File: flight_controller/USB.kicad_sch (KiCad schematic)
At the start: 11 parts, among them J17 TYPE-C16PIN2MD(073) (USB TYPE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, U15 SN74LVC1G07DBVR_C19829659

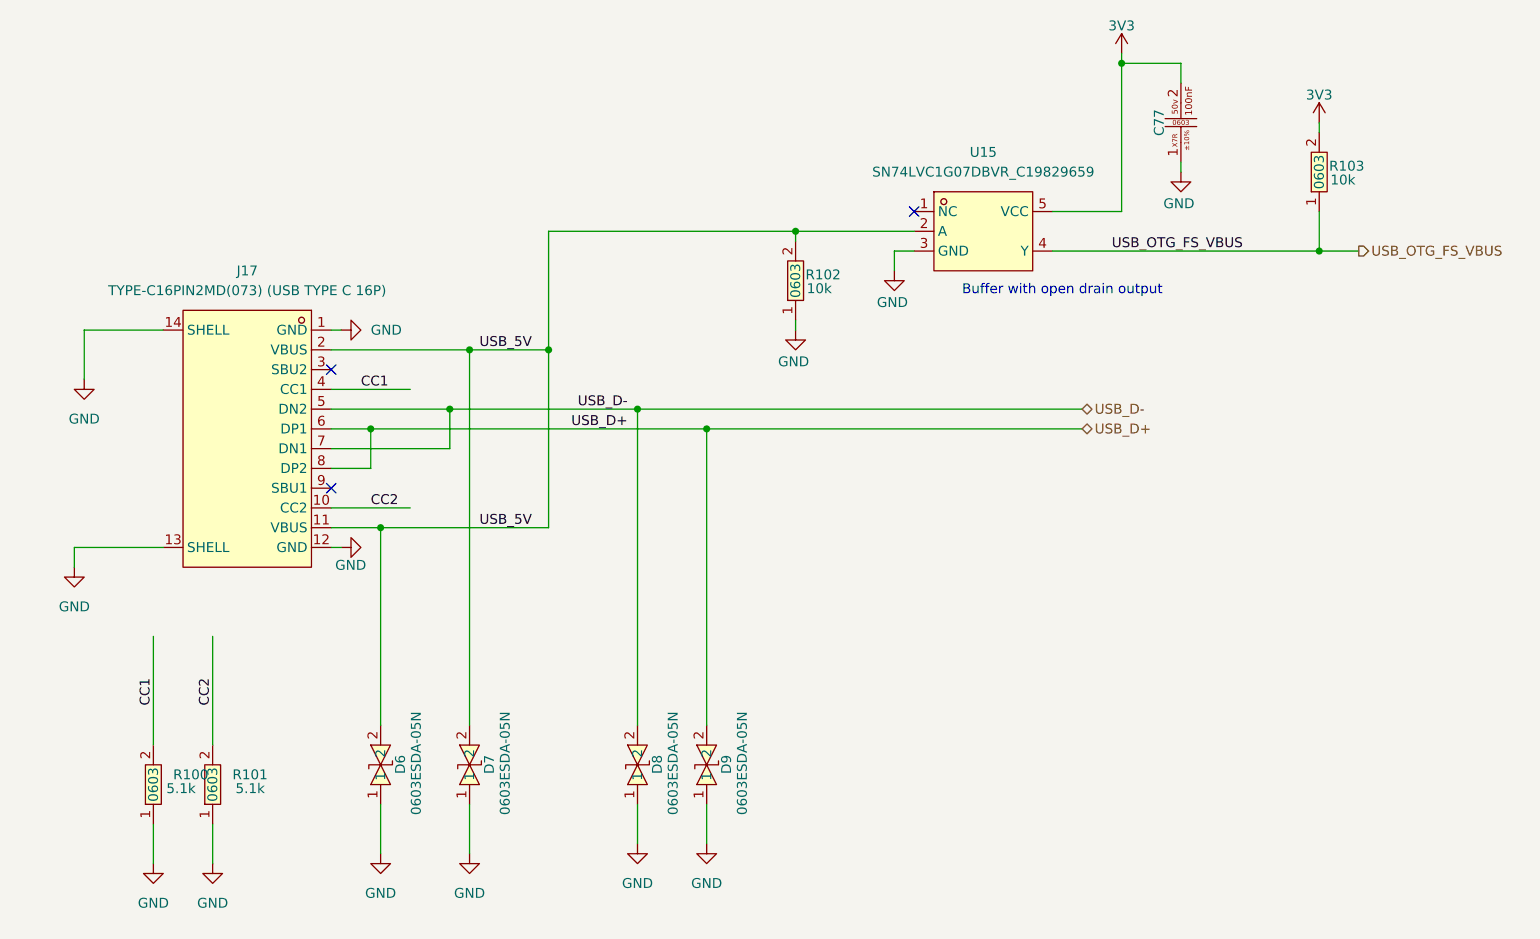
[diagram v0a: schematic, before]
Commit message: Updated power and usb connectors, annotations and netlist check
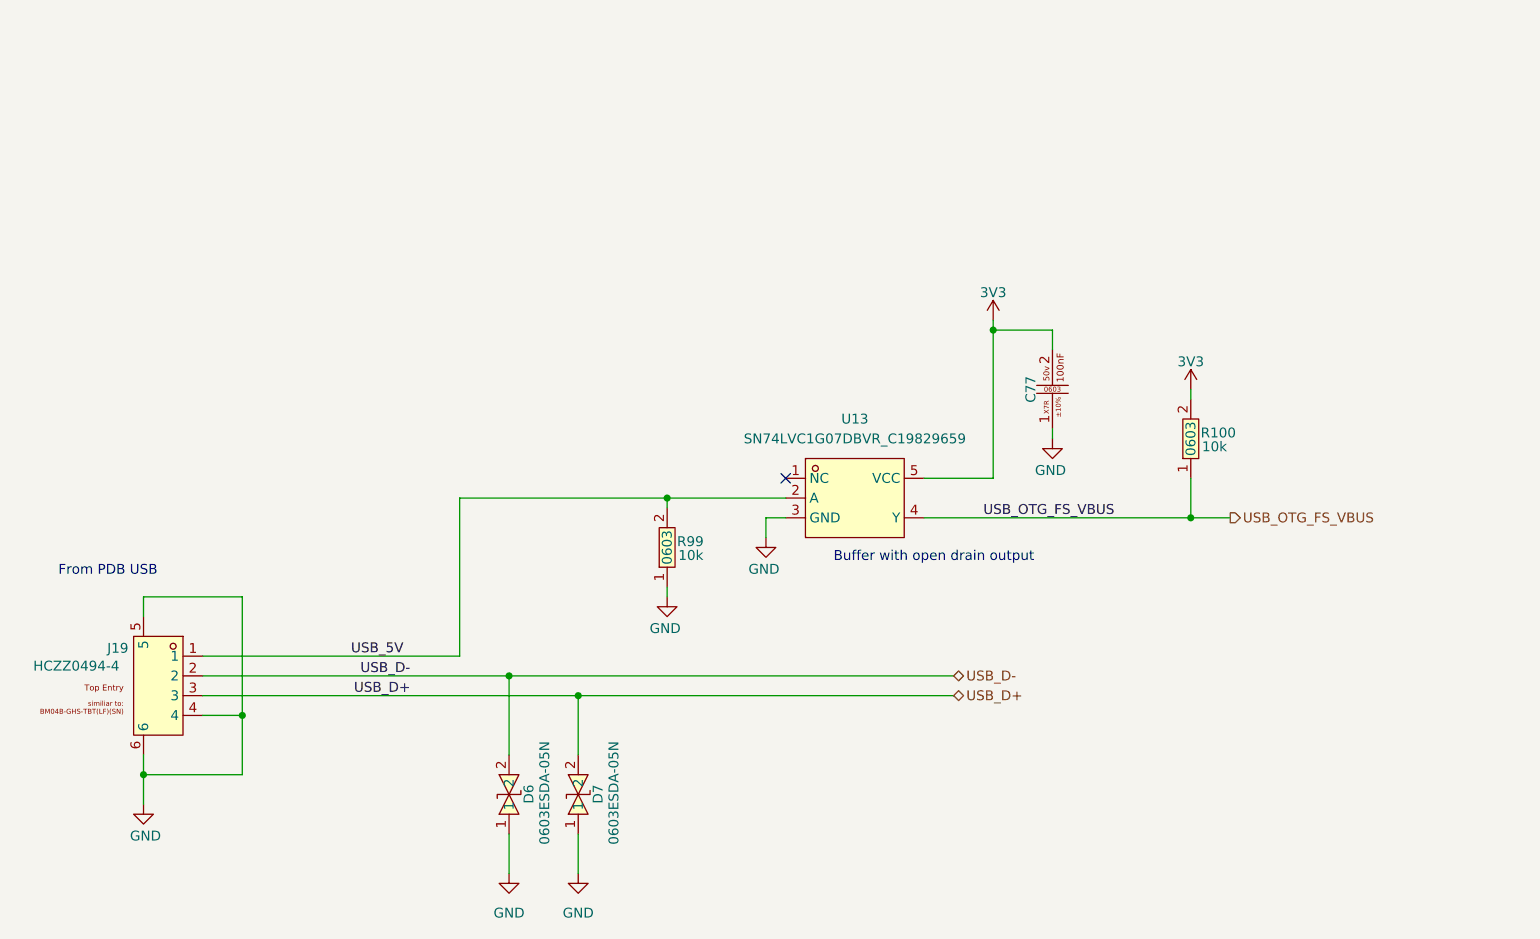
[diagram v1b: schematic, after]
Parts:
- removed D6, D7: 0603ESDA-05N, easyeda2kicad:D0603-BI, symbol easyeda2kicad:0603ESDA-05N
- removed J17: TYPE-C16PIN2MD(073) (USB TYPE C 16P), easyeda2kicad:USB-C-SMD_TYPE-C-6PIN-2MD-073, symbol lampelKicadLIB:TYPE-C16PIN2MD(073) (USB TYPE C 16P)
- removed R100, R101: 0603WAF5101T5E, easyeda2kicad:R0603, symbol easyeda2kicad:0603WAF5101T5E
- added J19: HCZZ0494-4, easyeda2kicad:CONN-SMD_4P-P1.25_BM04B-GHS-TBT-LF-SN, symbol lampelKicadLIB:HCZZ0494-4
- renumbered D8 to D6, D9 to D7, R103 to R100, R102 to R99, U15 to U13
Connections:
- net GND: now also J19.4, J19.5, J19.6
- net USB_5V: now also J19.1
- net USB_D+: now also J19.3
- net USB_D-: now also J19.2
- no-connect marks 3 -> 1
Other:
- note added: "From PDB USB"
- moved on the sheet: C77, D6, D7, R100, R99, U13

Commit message: Revert to state of commit 2458262 moved all to components to top
Reverts commits: d012532, 3d9c600, 58bc0ac
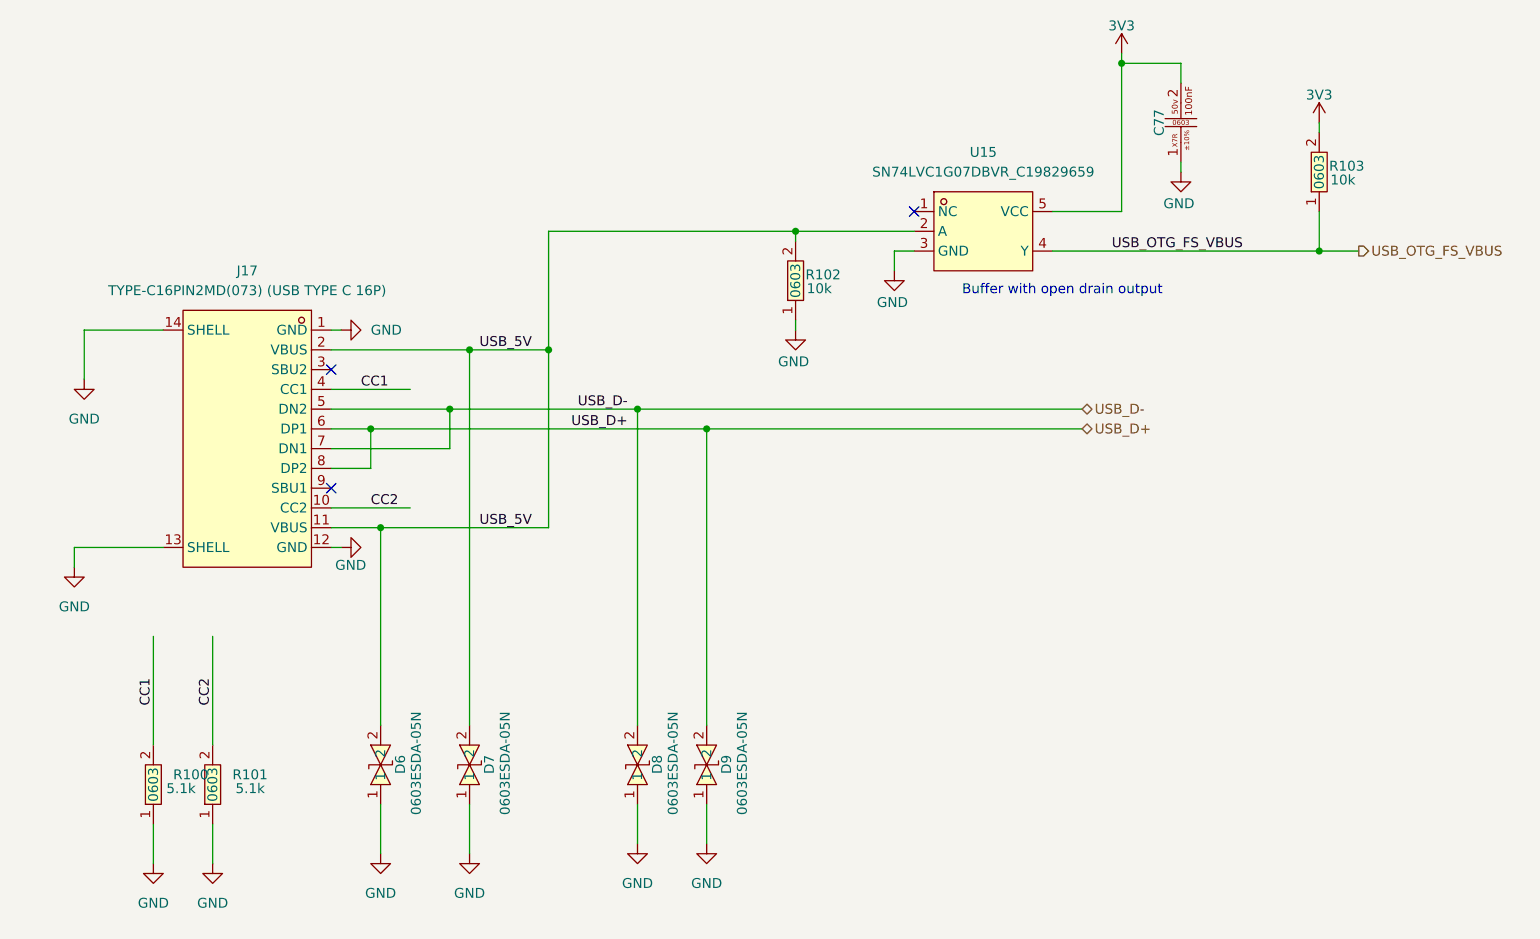
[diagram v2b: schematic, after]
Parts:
- removed J19: HCZZ0494-4, easyeda2kicad:CONN-SMD_4P-P1.25_BM04B-GHS-TBT-LF-SN, symbol lampelKicadLIB:HCZZ0494-4
- added D6, D7: 0603ESDA-05N, easyeda2kicad:D0603-BI, symbol easyeda2kicad:0603ESDA-05N
- added J17: TYPE-C16PIN2MD(073) (USB TYPE C 16P), easyeda2kicad:USB-C-SMD_TYPE-C-6PIN-2MD-073, symbol lampelKicadLIB:TYPE-C16PIN2MD(073) (USB TYPE C 16P)
- added R100, R101: 0603WAF5101T5E, easyeda2kicad:R0603, symbol easyeda2kicad:0603WAF5101T5E
- renumbered D6 to D8, D7 to D9, R99 to R102, R100 to R103, U13 to U15
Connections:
- net GND: now also D6.1, D7.1, J17.1 (GND), J17.12 (GND), J17.13 (SHELL), J17.14 (SHELL), R100.1, R101.1
- net USB_5V: now also D6.2, D7.2, J17.11 (VBUS), J17.2 (VBUS)
- net USB_D+: now also J17.6 (DP1), J17.8 (DP2)
- net USB_D-: now also J17.5 (DN2), J17.7 (DN1)
- new net CC1: J17.4 (CC1), R100.2
- new net CC2: J17.10 (CC2), R101.2
- no-connect marks 1 -> 3
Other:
- note removed: "From PDB USB"
- moved on the sheet: C77, D8, D9, R102, R103, U15
